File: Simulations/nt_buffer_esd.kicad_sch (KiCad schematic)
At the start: 19 parts, among them U1 MCP6021

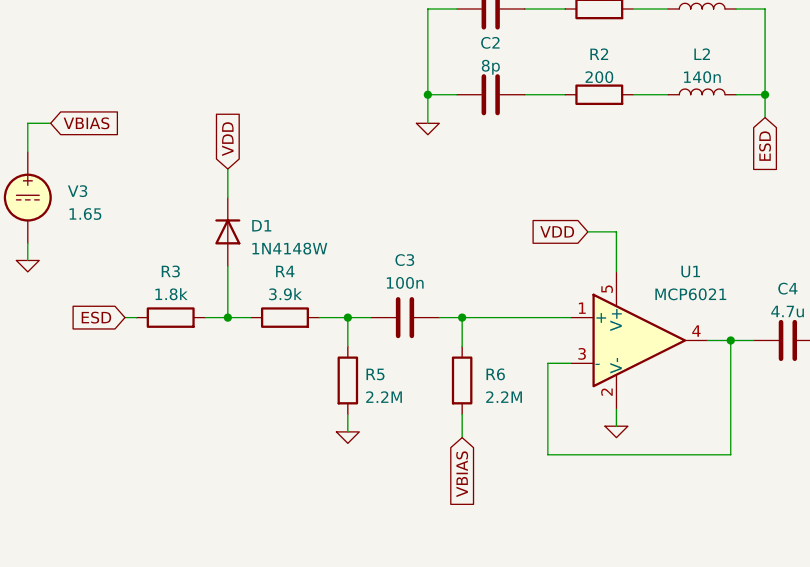
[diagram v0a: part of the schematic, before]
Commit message: change audio signal film cap to something more available
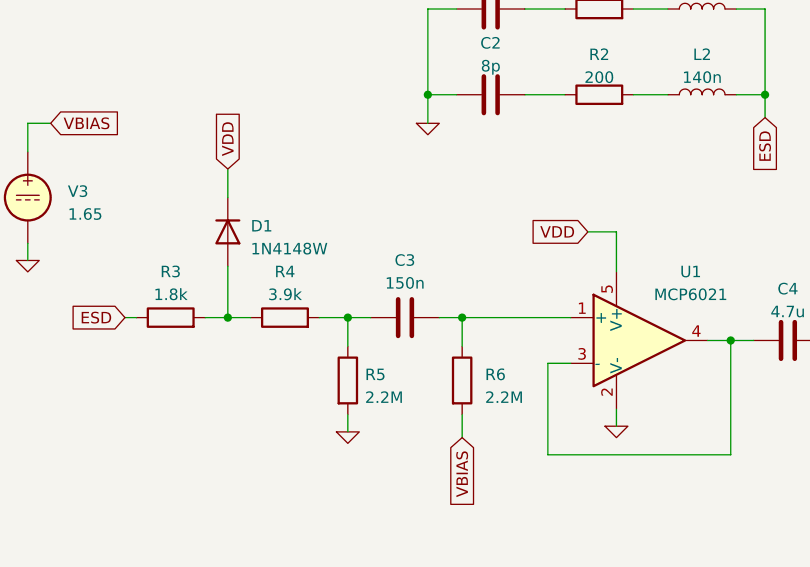
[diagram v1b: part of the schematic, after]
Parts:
- C3: value 100n -> 150n
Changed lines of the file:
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@@
       (effects (font (size 1.27 1.27)))
     )
-    (property "Value" "100n" (at 133.985 93.98 90)
+    (property "Value" "150n" (at 133.985 93.98 90)
       (effects (font (size 1.27 1.27)))
     )

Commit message: cleanup and lcsc part numbers
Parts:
- removed R5: 2.2M, symbol Device:R
- removed R8: 100, symbol Device:R
- C3: value 150n -> 100n
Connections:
- net OUT: now also C4.2, R7.1
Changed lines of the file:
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@@
   (junction (at 140.335 97.79) (diameter 0) (color 0 0 0 0)
   )
-  (junction (at 127.635 97.79) (diameter 0) (color 0 0 0 0)
-  )
   (junction (at 136.525 73.025) (diameter 0) (color 0 0 0 0)
   )
-  (wire (pts (xy 127.635 108.585) (xy 127.635 110.49))
-    (stroke (width 0) (type default))
-  )
   (wire (pts (xy 76.835 76.2) (xy 79.375 76.2))
     (stroke (width 0) (type default))
@@
     (stroke (width 0) (type default))
   )
-  (wire (pts (xy 193.675 100.33) (xy 196.215 100.33))
-    (stroke (width 0) (type default))
-  )
   (wire (pts (xy 170.815 63.5) (xy 173.99 63.5))
     (stroke (width 0) (type default))
@@
     (stroke (width 0) (type default))
   )
-  (wire (pts (xy 127.635 97.79) (xy 130.175 97.79))
-    (stroke (width 0) (type default))
-  )
   (wire (pts (xy 140.335 100.965) (xy 140.335 97.79))
     (stroke (width 0) (type default))
   )
-  (wire (pts (xy 127.635 97.79) (xy 127.635 100.965))
-    (stroke (width 0) (type default))
-  )
   (wire (pts (xy 170.18 113.03) (xy 170.18 100.33))
     (stroke (width 0) (type default))
@@
     (stroke (width 0) (type default))
   )
-  (wire (pts (xy 183.515 100.33) (xy 186.055 100.33))
+  (wire (pts (xy 183.515 100.33) (xy 196.215 100.33))
     (stroke (width 0) (type default))
   )
@@
     (stroke (width 0) (type default))
   )
-  (wire (pts (xy 124.46 97.79) (xy 127.635 97.79))
+  (wire (pts (xy 124.46 97.79) (xy 130.175 97.79))
     (stroke (width 0) (type default))
   )
@@
     )
   )
-  (symbol (lib_id "Device:R") (at 127.635 104.775 0) (unit 1)
-    (in_bom yes) (on_board yes) (dnp no) (fields_autoplaced)
-    (property "Reference" "R5" (at 129.54 104.14 0)
-      (effects (font (size 1.27 1.27)) (justify left))
-    )
-    (property "Value" "2.2M" (at 129.54 106.68 0)
-      (effects (font (size 1.27 1.27)) (justify left))
-    )
-    (property "Footprint" "" (at 125.857 104.775 90)
-      (effects (font (size 1.27 1.27)) hide)
-    )
-    (property "Datasheet" "~" (at 127.635 104.775 0)
-      (effects (font (size 1.27 1.27)) hide)
-    )
-    (pin "1")
-    (pin "2")
-    (instances
-      (project "nt_buffer_esd"
-        (path "/ea4fc8d5-926a-4e1e-b9cd-45e6fdca0bc8"
-          (reference "R5") (unit 1)
-        )
-      )
-    )
-  )
-  (symbol (lib_id "Simulation_SPICE:0") (at 127.635 110.49 0) (unit 1)
-    (in_bom yes) (on_board yes) (dnp no) (fields_autoplaced)
-    (property "Reference" "#GND05" (at 127.635 113.03 0)
-      (effects (font (size 1.27 1.27)) hide)
-    )
-    (property "Value" "0" (at 127.635 109.855 0)
-      (effects (font (size 1.27 1.27)) hide)
-    )
-    (property "Footprint" "" (at 127.635 110.49 0)
-      (effects (font (size 1.27 1.27)) hide)
-    )
-    (property "Datasheet" "~" (at 127.635 110.49 0)
-      (effects (font (size 1.27 1.27)) hide)
-    )
-    (pin "1")
-    (instances
-      (project "nt_buffer_esd"
-        (path "/ea4fc8d5-926a-4e1e-b9cd-45e6fdca0bc8"
-          (reference "#GND05") (unit 1)
-        )
-      )
-    )
-  )
   (symbol (lib_id "Simulation_SPICE:0") (at 92.075 91.44 0) (unit 1)
     (in_bom yes) (on_board yes) (dnp no) (fields_autoplaced)
@@
         (path "/ea4fc8d5-926a-4e1e-b9cd-45e6fdca0bc8"
           (reference "#GND03") (unit 1)
-        )
-      )
-    )
-  )
-  (symbol (lib_id "Device:R") (at 189.865 100.33 90) (unit 1)
-    (in_bom yes) (on_board yes) (dnp no) (fields_autoplaced)
-    (property "Reference" "R8" (at 189.865 95.885 90)
-      (effects (font (size 1.27 1.27)))
-    )
-    (property "Value" "100" (at 189.865 98.425 90)
-      (effects (font (size 1.27 1.27)))
-    )
-    (property "Footprint" "" (at 189.865 102.108 90)
-      (effects (font (size 1.27 1.27)) hide)
-    )
-    (property "Datasheet" "~" (at 189.865 100.33 0)
-      (effects (font (size 1.27 1.27)) hide)
-    )
-    (pin "1")
-    (pin "2")
-    (instances
-      (project "nt_buffer_esd"
-        (path "/ea4fc8d5-926a-4e1e-b9cd-45e6fdca0bc8"
-          (reference "R8") (unit 1)
         )
       )
@@
       (effects (font (size 1.27 1.27)))
     )
-    (property "Value" "150n" (at 133.985 93.98 90)
-      (effects (font (size 1.27 1.27)))
-    )
+    (property "Value" "100n" (at 133.985 93.98 90)
+      (effects (font (size 1.27 1.27)))
+    )
